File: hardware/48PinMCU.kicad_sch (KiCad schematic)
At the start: 34 parts, among them J6 SWD_Header, J7 SWD, SW1 Reset, SW2 SW_SPDT, U6 STM32G473CETx, Y1 Crystal

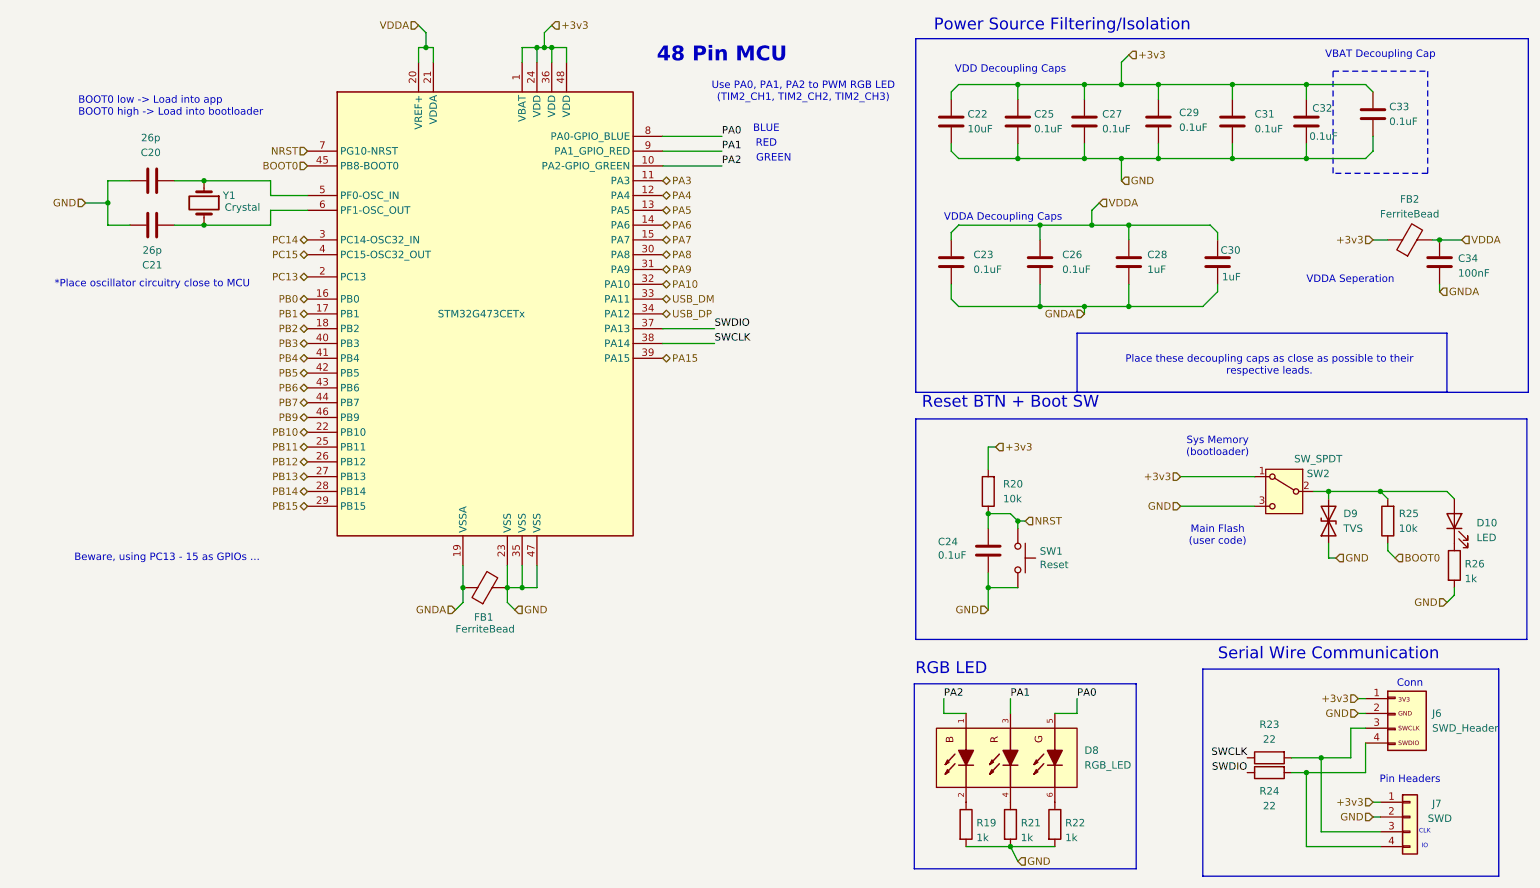
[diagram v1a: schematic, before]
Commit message: reduce op amps, better hierarchal
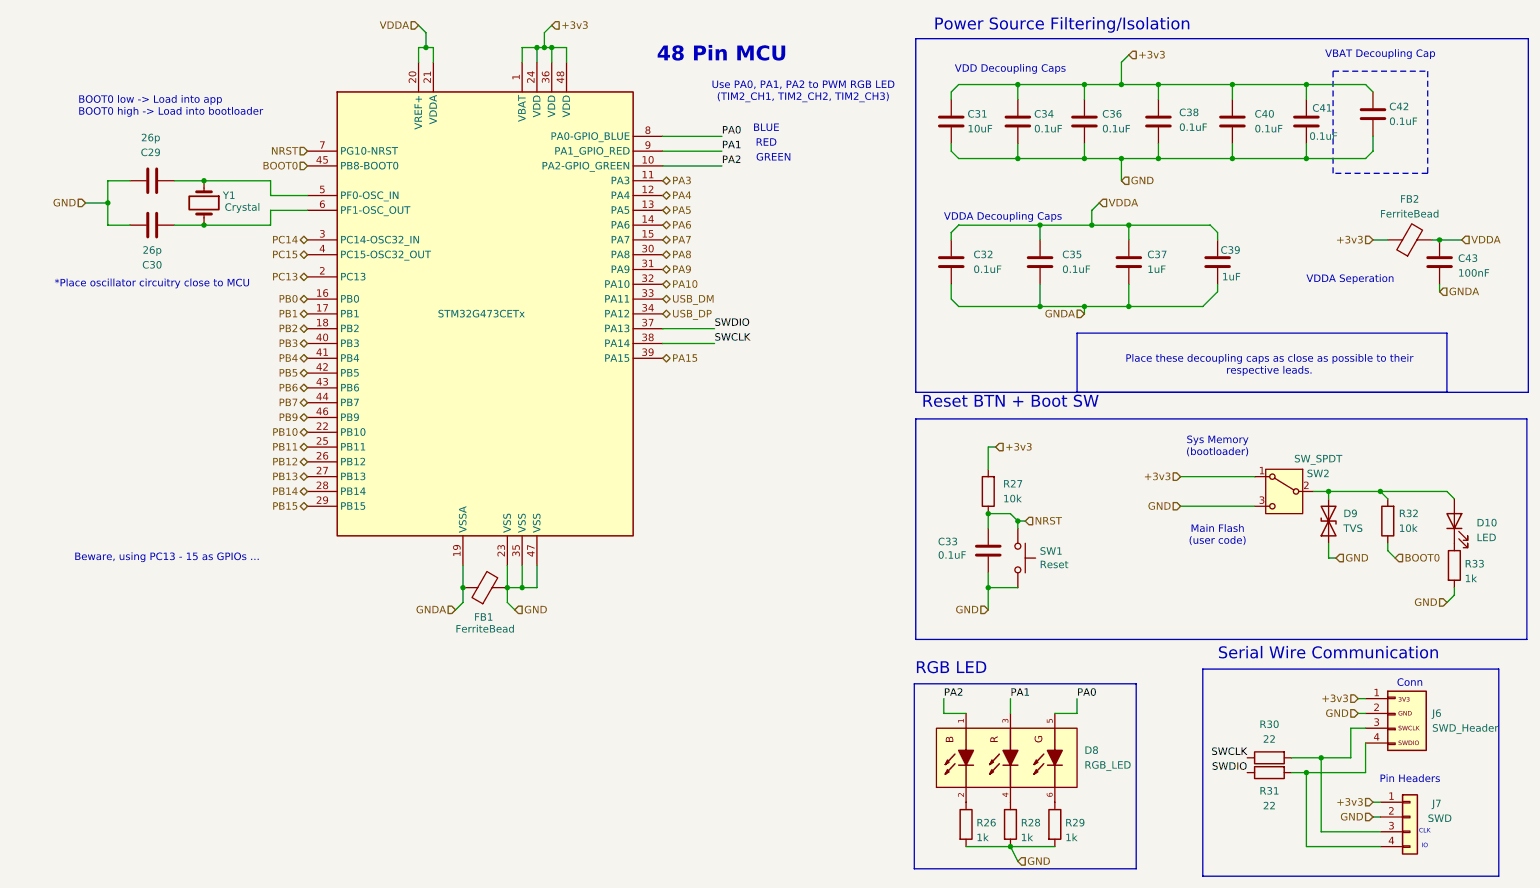
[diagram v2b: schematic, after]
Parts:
- renumbered C20 to C29, C21 to C30, C22 to C31, C23 to C32, C24 to C33, C25 to C34, C26 to C35, C27 to C36, C28 to C37, C29 to C38, C30 to C39, C31 to C40, C32 to C41, C33 to C42, C34 to C43, R19 to R26, R20 to R27, R21 to R28, R22 to R29, R23 to R30, R24 to R31, R25 to R32, R26 to R33, U6 to U7
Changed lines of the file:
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@@
 		(dnp no)
 		(fields_autoplaced yes)
-		(property "Reference" "C26"
+		(property "Reference" "C35"
 			(at 190.5 57.1499 0)
 			(show_name no)
@@
 			(project "PS-HVCarrier"
 				(path "/2365a867-6254-4a7c-9718-f325e0bbac5c/525eebd7-cd9b-471b-950d-358e3ce0c5f6"
-					(reference "C26")
+					(reference "C35")
 					(unit 1)
 				)
@@
 		(in_pos_files yes)
 		(dnp no)
-		(property "Reference" "R21"
+		(property "Reference" "R28"
 			(at 183.388 154.686 0)
 			(show_name no)
@@
 			(project "PS-HVCarrier"
 				(path "/2365a867-6254-4a7c-9718-f325e0bbac5c/525eebd7-cd9b-471b-950d-358e3ce0c5f6"
-					(reference "R21")
+					(reference "R28")
 					(unit 1)
 				)
@@
 		(in_pos_files yes)
 		(dnp no)
-		(property "Reference" "U6"
+		(property "Reference" "U7"
 			(at 88.392 73.66 0)
 			(hide yes)
@@
 			(project "PS-HVCarrier"
 				(path "/2365a867-6254-4a7c-9718-f325e0bbac5c/525eebd7-cd9b-471b-950d-358e3ce0c5f6"
-					(reference "U6")
+					(reference "U7")
 					(unit 1)
 				)
@@
 		(in_pos_files yes)
 		(dnp no)
-		(property "Reference" "C33"
+		(property "Reference" "C42"
 			(at 246.634 31.75 0)
 			(show_name no)
@@
 			(project "PS-HVCarrier"
 				(path "/2365a867-6254-4a7c-9718-f325e0bbac5c/525eebd7-cd9b-471b-950d-358e3ce0c5f6"
-					(reference "C33")
+					(reference "C42")
 					(unit 1)
 				)
@@
 		(dnp no)
 		(fields_autoplaced yes)
-		(property "Reference" "C28"
+		(property "Reference" "C37"
 			(at 205.105 57.1499 0)
 			(show_name no)
@@
 			(project "PS-HVCarrier"
 				(path "/2365a867-6254-4a7c-9718-f325e0bbac5c/525eebd7-cd9b-471b-950d-358e3ce0c5f6"
-					(reference "C28")
+					(reference "C37")
 					(unit 1)
 				)
@@
 		(dnp no)
 		(fields_autoplaced yes)
-		(property "Reference" "C31"
+		(property "Reference" "C40"
 			(at 223.52 33.0199 0)
 			(show_name no)
@@
 			(project "PS-HVCarrier"
 				(path "/2365a867-6254-4a7c-9718-f325e0bbac5c/525eebd7-cd9b-471b-950d-358e3ce0c5f6"
-					(reference "C31")
+					(reference "C40")
 					(unit 1)
 				)
@@
 		(in_pos_files yes)
 		(dnp no)
-		(property "Reference" "C29"
+		(property "Reference" "C38"
 			(at 210.566 32.766 0)
 			(show_name no)
@@
 			(project "PS-HVCarrier"
 				(path "/2365a867-6254-4a7c-9718-f325e0bbac5c/525eebd7-cd9b-471b-950d-358e3ce0c5f6"
-					(reference "C29")
+					(reference "C38")
 					(unit 1)
 				)
@@
 		(in_pos_files yes)
 		(dnp no)
-		(property "Reference" "C25"
+		(property "Reference" "C34"
 			(at 185.674 33.02 0)
 			(show_name no)
@@
 			(project "PS-HVCarrier"
 				(path "/2365a867-6254-4a7c-9718-f325e0bbac5c/525eebd7-cd9b-471b-950d-358e3ce0c5f6"
-					(reference "C25")
+					(reference "C34")
 					(unit 1)
 				)
@@
 		(dnp no)
 		(fields_autoplaced yes)
-		(property "Reference" "C34"
+		(property "Reference" "C43"
 			(at 258.445 57.785 0)
 			(show_name no)
@@
 			(project "PS-HVCarrier"
 				(path "/2365a867-6254-4a7c-9718-f325e0bbac5c/525eebd7-cd9b-471b-950d-358e3ce0c5f6"
-					(reference "C34")
+					(reference "C43")
 					(unit 1)
 				)
@@
 		(in_pos_files yes)
 		(dnp no)
-		(property "Reference" "C27"
+		(property "Reference" "C36"
 			(at 197.358 33.02 0)
 			(show_name no)
@@
 			(project "PS-HVCarrier"
 				(path "/2365a867-6254-4a7c-9718-f325e0bbac5c/525eebd7-cd9b-471b-950d-358e3ce0c5f6"
-					(reference "C27")
+					(reference "C36")
 					(unit 1)
 				)
@@
 		(in_pos_files yes)
 		(dnp no)
-		(property "Reference" "C30"
+		(property "Reference" "C39"
 			(at 217.678 56.388 0)
 			(show_name no)
@@
 			(project "PS-HVCarrier"
 				(path "/2365a867-6254-4a7c-9718-f325e0bbac5c/525eebd7-cd9b-471b-950d-358e3ce0c5f6"
-					(reference "C30")
+					(reference "C39")
 					(unit 1)
 				)
@@
 		(in_pos_files yes)
 		(dnp no)
-		(property "Reference" "R22"
+		(property "Reference" "R29"
 			(at 191.008 154.686 0)
 			(show_name no)
@@
 			(project "PS-HVCarrier"
 				(path "/2365a867-6254-4a7c-9718-f325e0bbac5c/525eebd7-cd9b-471b-950d-358e3ce0c5f6"
-					(reference "R22")
+					(reference "R29")
 					(unit 1)
 				)
@@
 		(in_pos_files yes)
 		(dnp no)
-		(property "Reference" "R26"
+		(property "Reference" "R33"
 			(at 259.588 110.236 0)
 			(show_name no)
@@
 			(project "PS-HVCarrier"
 				(path "/2365a867-6254-4a7c-9718-f325e0bbac5c/525eebd7-cd9b-471b-950d-358e3ce0c5f6"
-					(reference "R26")
+					(reference "R33")
 					(unit 1)
 				)
@@
 		(in_pos_files yes)
 		(dnp no)
-		(property "Reference" "C20"
+		(property "Reference" "C29"
 			(at 34.036 39.624 90)
 			(show_name no)
@@
 			(project "PS-HVCarrier"
 				(path "/2365a867-6254-4a7c-9718-f325e0bbac5c/525eebd7-cd9b-471b-950d-358e3ce0c5f6"
-					(reference "C20")
+					(reference "C29")
 					(unit 1)
 				)
@@
 		(dnp no)
 		(fields_autoplaced yes)
-		(property "Reference" "C23"
+		(property "Reference" "C32"
 			(at 175.26 57.1499 0)
 			(show_name no)
@@
 			(project "PS-HVCarrier"
 				(path "/2365a867-6254-4a7c-9718-f325e0bbac5c/525eebd7-cd9b-471b-950d-358e3ce0c5f6"
-					(reference "C23")
+					(reference "C32")
 					(unit 1)
 				)
@@
 		(dnp no)
 		(fields_autoplaced yes)
-		(property "Reference" "R20"
+		(property "Reference" "R27"
 			(at 180.34 96.5199 0)
 			(show_name no)
@@
 			(project "PS-HVCarrier"
 				(path "/2365a867-6254-4a7c-9718-f325e0bbac5c/525eebd7-cd9b-471b-950d-358e3ce0c5f6"
-					(reference "R20")
+					(reference "R27")
 					(unit 1)
 				)
@@
 		(in_pos_files yes)
 		(dnp no)
-		(property "Reference" "R19"
+		(property "Reference" "R26"
 			(at 175.768 154.686 0)
 			(show_name no)
@@
 			(project "PS-HVCarrier"
 				(path "/2365a867-6254-4a7c-9718-f325e0bbac5c/525eebd7-cd9b-471b-950d-358e3ce0c5f6"
-					(reference "R19")
+					(reference "R26")
 					(unit 1)
 				)
@@
 		(in_pos_files yes)
 		(dnp no)
-		(property "Reference" "R24"
+		(property "Reference" "R31"
 			(at 226.06 149.225 90)
 			(show_name no)
@@
 			(project "PS-HVCarrier"
 				(path "/2365a867-6254-4a7c-9718-f325e0bbac5c/525eebd7-cd9b-471b-950d-358e3ce0c5f6"
-					(reference "R24")
+					(reference "R31")
 					(unit 1)
 				)
@@
 		(in_pos_files yes)
 		(dnp no)
-		(property "Reference" "C22"
+		(property "Reference" "C31"
 			(at 174.244 33.02 0)
 			(show_name no)
@@
 			(project "PS-HVCarrier"
 				(path "/2365a867-6254-4a7c-9718-f325e0bbac5c/525eebd7-cd9b-471b-950d-358e3ce0c5f6"
-					(reference "C22")
+					(reference "C31")
 					(unit 1)
 				)
@@
 		(in_pos_files yes)
 		(dnp no)
-		(property "Reference" "R25"
+		(property "Reference" "R32"
 			(at 248.285 101.5999 0)
 			(show_name no)
@@
 			(project "PS-HVCarrier"
 				(path "/2365a867-6254-4a7c-9718-f325e0bbac5c/525eebd7-cd9b-471b-950d-358e3ce0c5f6"
-					(reference "R25")
+					(reference "R32")
 					(unit 1)
 				)
@@
 		(dnp no)
 		(fields_autoplaced yes)
-		(property "Reference" "C21"
+		(property "Reference" "C30"
 			(at 34.29 58.928 90)
 			(show_name no)
@@
 			(project "PS-HVCarrier"
 				(path "/2365a867-6254-4a7c-9718-f325e0bbac5c/525eebd7-cd9b-471b-950d-358e3ce0c5f6"
-					(reference "C21")
+					(reference "C30")
 					(unit 1)
 				)
@@
 		(in_pos_files yes)
 		(dnp no)
-		(property "Reference" "C24"
+		(property "Reference" "C33"
 			(at 169.164 106.426 0)
 			(show_name no)
@@
 			(project "PS-HVCarrier"
 				(path "/2365a867-6254-4a7c-9718-f325e0bbac5c/525eebd7-cd9b-471b-950d-358e3ce0c5f6"
-					(reference "C24")
+					(reference "C33")
 					(unit 1)
 				)
@@
 		(dnp no)
 		(fields_autoplaced yes)
-		(property "Reference" "R23"
+		(property "Reference" "R30"
 			(at 226.06 137.795 90)
 			(show_name no)
@@
 			(project "PS-HVCarrier"
 				(path "/2365a867-6254-4a7c-9718-f325e0bbac5c/525eebd7-cd9b-471b-950d-358e3ce0c5f6"
-					(reference "R23")
+					(reference "R30")
 					(unit 1)
 				)
@@
 		(in_pos_files yes)
 		(dnp no)
-		(property "Reference" "C32"
+		(property "Reference" "C41"
 			(at 233.426 32.004 0)
 			(show_name no)
@@
 			(project "PS-HVCarrier"
 				(path "/2365a867-6254-4a7c-9718-f325e0bbac5c/525eebd7-cd9b-471b-950d-358e3ce0c5f6"
-					(reference "C32")
+					(reference "C41")
 					(unit 1)
 				)
